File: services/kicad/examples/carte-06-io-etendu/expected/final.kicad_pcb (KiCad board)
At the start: 2 copper layers, 80 x 60 mm, 35 parts, among them J1 IN_5V, J2 SWD, J3 IO0, J4 IO1, U1 STM32F103C8T6, U2 AMS1117-3.3

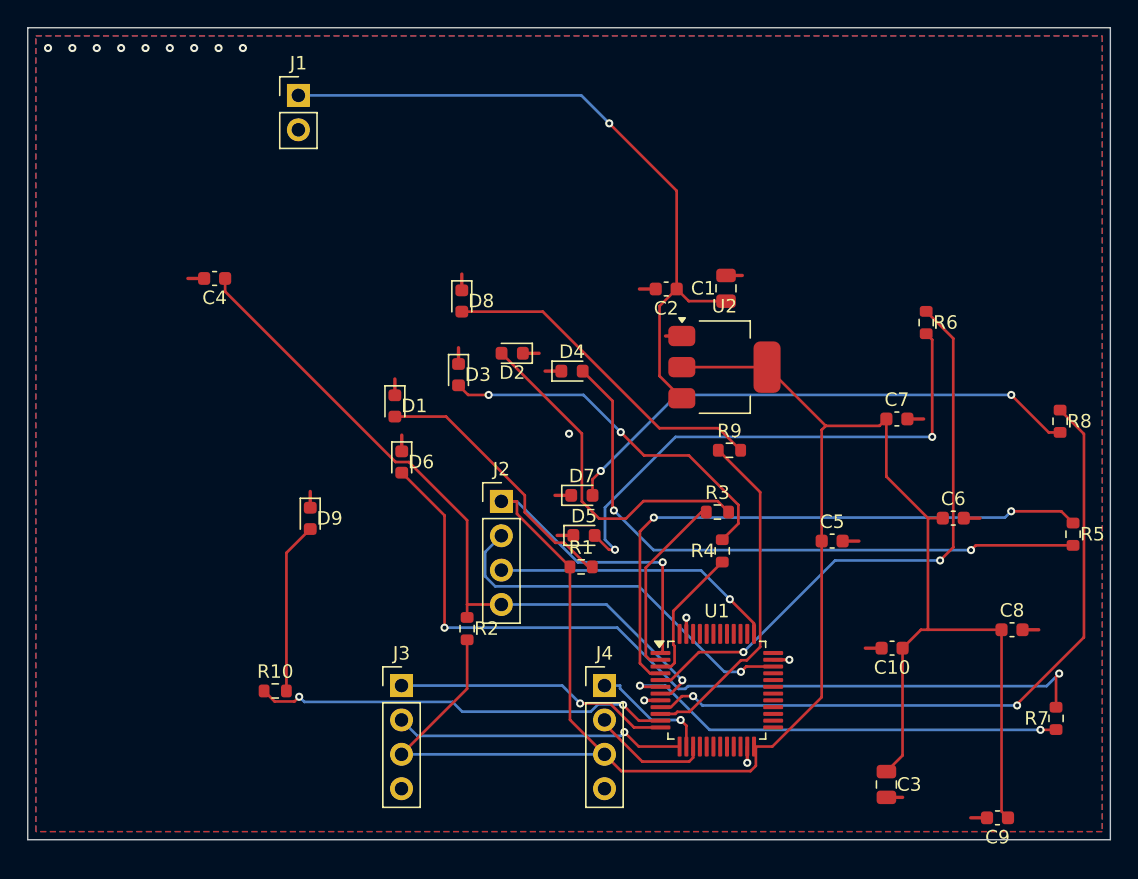
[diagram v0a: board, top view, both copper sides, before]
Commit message: test(examples): banc regenere -- placements livres, journaux et mesures a jour
- expected/placement.kicad_pcb ajoutes (carte-05, carte-06) et
  vue-dessus.png (carte-04) : le banc compare desormais le placement,
  pas seulement le board final.
- generer_exemples.py, regenerer_le_banc.py, livrer_placements.py,
  apercu_routage.py : regeneration reproductible du banc et rendus
  d apercu.
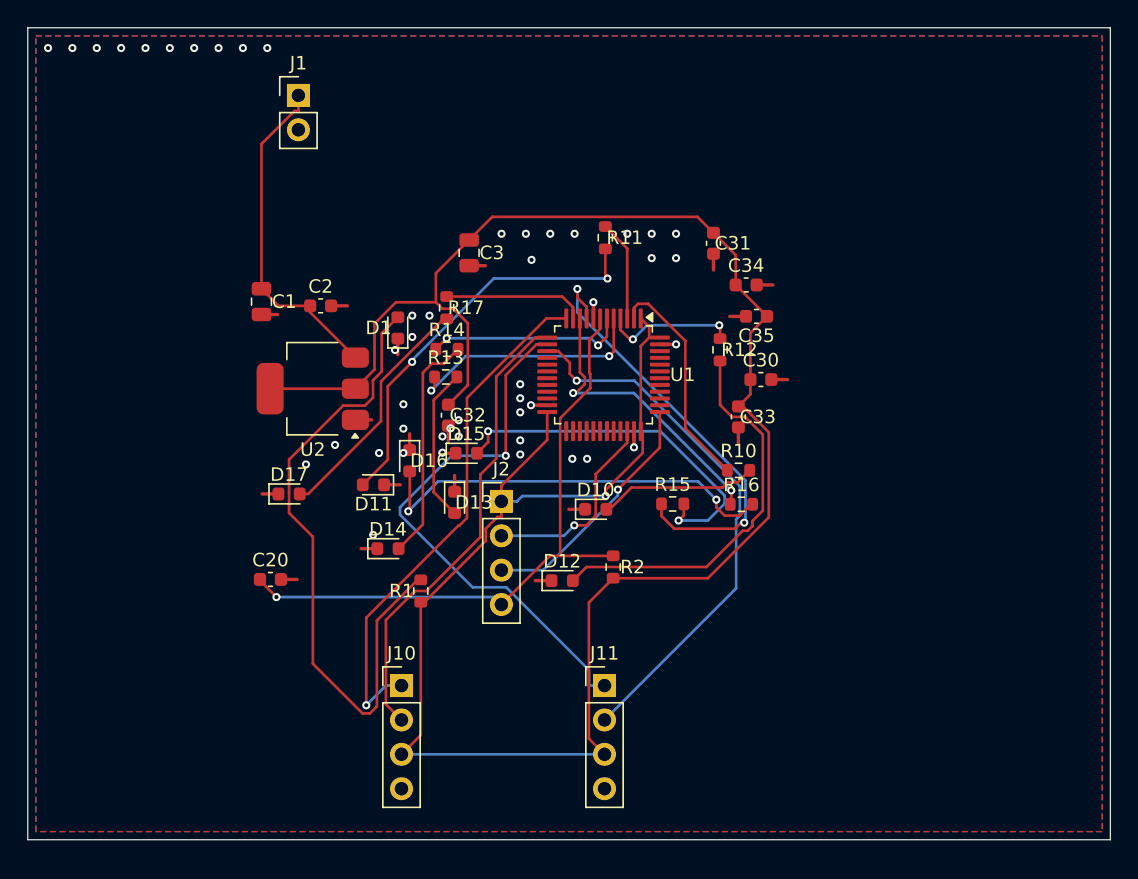
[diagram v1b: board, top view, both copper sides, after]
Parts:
- removed C10, C4, C5, C6, C7, C8, C9: 100nF, C_0603_1608Metric
- removed D2, D3, D4, D5, D6, D7, D8, D9: LED, LED_0603_1608Metric
- removed J3: IO0, PinHeader_1x04_P2.54mm_Vertical
- removed J4: IO1, PinHeader_1x04_P2.54mm_Vertical
- removed R3, R4, R5, R6, R7, R8, R9: 1k, R_0603_1608Metric
- added C20: 100nF, C_0603_1608Metric, F.Cu at (126.4, 115.8)
- added C30: 100nF, C_0603_1608Metric, F.Cu at (162.7, 101.0)
- added C31: 100nF, C_0603_1608Metric, F.Cu at (159.2, 90.9)
- added C32: 100nF, C_0603_1608Metric, F.Cu at (139.6, 103.6)
- added C33: 100nF, C_0603_1608Metric, F.Cu at (161.0, 103.8)
- added C34: 100nF, C_0603_1608Metric, F.Cu at (161.6, 94.0)
- added C35: 100nF, C_0603_1608Metric, F.Cu at (162.3, 96.3)
- added D10: LED, LED_0603_1608Metric, F.Cu at (150.5, 110.6)
- added D11: LED, LED_0603_1608Metric, F.Cu at (134.0, 108.8)
- added D12: LED, LED_0603_1608Metric, F.Cu at (148.0, 115.9)
- added D13: LED, LED_0603_1608Metric, F.Cu at (140.0, 110.1)
- added D14: LED, LED_0603_1608Metric, F.Cu at (135.1, 113.5)
- added D15: LED, LED_0603_1608Metric, F.Cu at (140.9, 106.4)
- added D16: LED, LED_0603_1608Metric, F.Cu at (136.7, 107.0)
- added D17: LED, LED_0603_1608Metric, F.Cu at (127.8, 109.5)
- added J10: IO0, PinHeader_1x04_P2.54mm_Vertical, F.Cu at (136.1, 123.6)
- added J11: IO1, PinHeader_1x04_P2.54mm_Vertical, F.Cu at (151.1, 123.6)
- added R11: 1k, R_0603_1608Metric, F.Cu at (151.2, 90.5)
- added R12: 1k, R_0603_1608Metric, F.Cu at (159.7, 98.8)
- added R13: 1k, R_0603_1608Metric, F.Cu at (139.4, 100.8)
- added R14: 1k, R_0603_1608Metric, F.Cu at (139.5, 98.8)
- added R15: 1k, R_0603_1608Metric, F.Cu at (156.2, 110.2)
- added R16: 1k, R_0603_1608Metric, F.Cu at (161.2, 110.2)
- added R17: 1k, R_0603_1608Metric, F.Cu at (139.5, 95.7)
- moved C3 49.9 mm to (141.1, 91.6)
- moved R10 37.9 mm to (161.0, 107.7)
- moved C1 34.3 mm to (125.8, 95.2), turned to -90 degrees
- moved U2 30.5 mm to (129.6, 101.7), turned to 180 degrees
- moved C2 25.6 mm to (130.1, 95.6), turned to 0 degrees
- moved U1 24.8 mm to (151.0, 100.6), turned to -90 degrees
- moved R1 12.0 mm to (137.5, 116.6), turned to 90 degrees
- moved R2 11.7 mm to (151.8, 114.9)
- moved D1 5.77 mm to (135.8, 97.2), turned to 90 degrees
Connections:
- R10 pad 1: IO_L7 -> IO_L0
- R10 pad 2: LEDA7 -> LEDA0
- U1 pad 36: Net-(U1-36) -> +3V3
- U1 pad 48: Net-(U1-48) -> +3V3
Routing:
- net LEDA4: track 63.1 -> 17.1 mm, vias 2 -> 0
- net IO_L2: track 44.5 -> 9.88 mm
- net EXT1_1: track 8.94 -> 40.9 mm
- net EXT1_2: track 8.93 -> 40.3 mm, vias 0 -> 1
- net LEDA3: track 39.5 -> 11.4 mm, vias 2 -> 0
- net LED_PWR: track 19.9 -> 47.9 mm
- net VIN: track 51.4 -> 24.9 mm, vias 1 -> 0
- net IO_L3: track 44.0 -> 18.2 mm
- net IO_L7: track 30.9 -> 10.5 mm, vias 2 -> 0
- net IO_L5: track 51.6 -> 32.5 mm
- net IO_L4: track 33.7 -> 14.8 mm
- net EXT0_1: track 20.4 -> 38.8 mm
- net LEDA2: track 46.5 -> 29.3 mm, vias 2 -> 0
- net LEDA0: track 25.6 -> 11.8 mm
- net EXT0_2: track 21.6 -> 34.7 mm, vias 1 -> 0
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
